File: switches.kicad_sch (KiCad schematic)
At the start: 134 parts

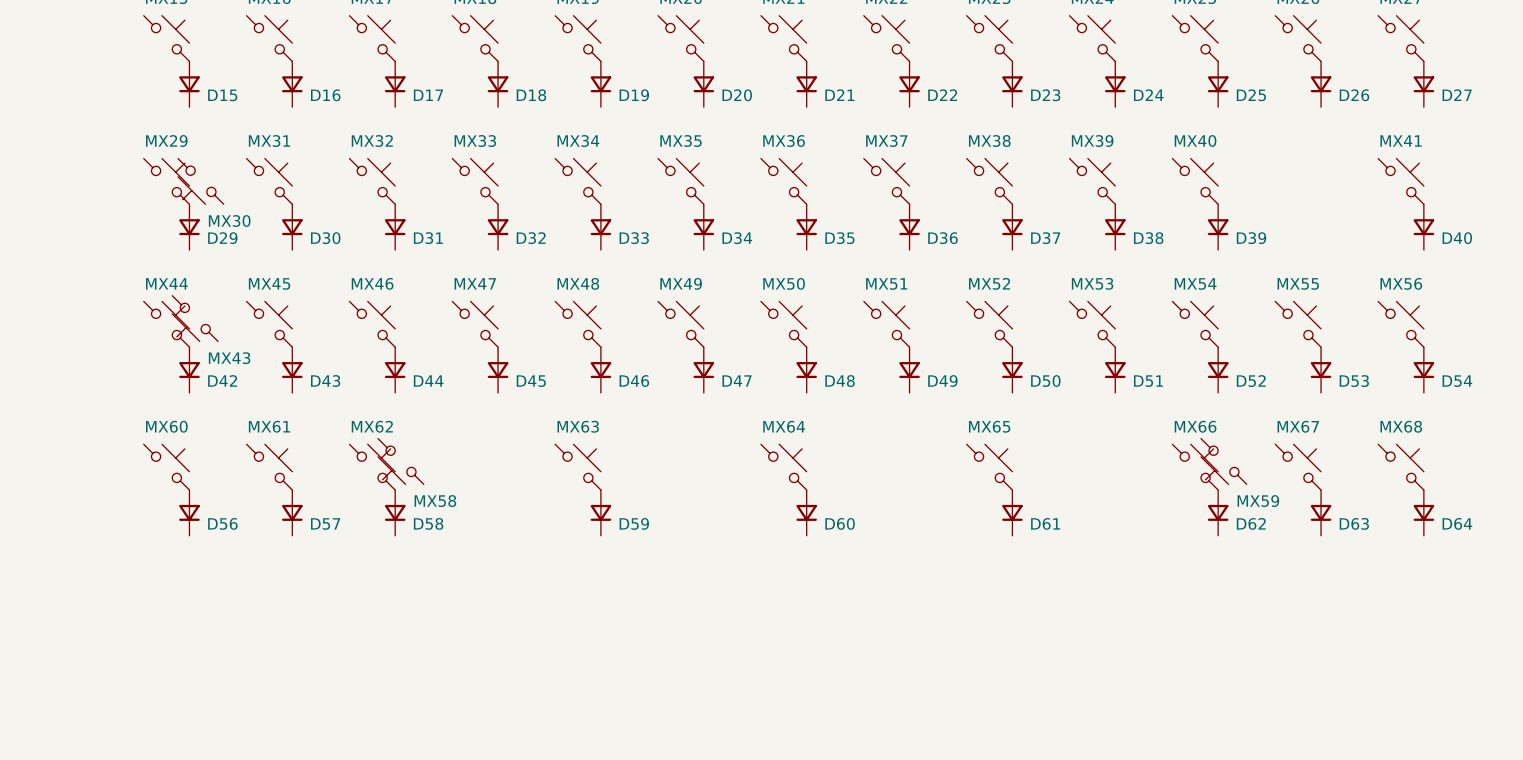
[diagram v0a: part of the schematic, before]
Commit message: Update PCB from schematics
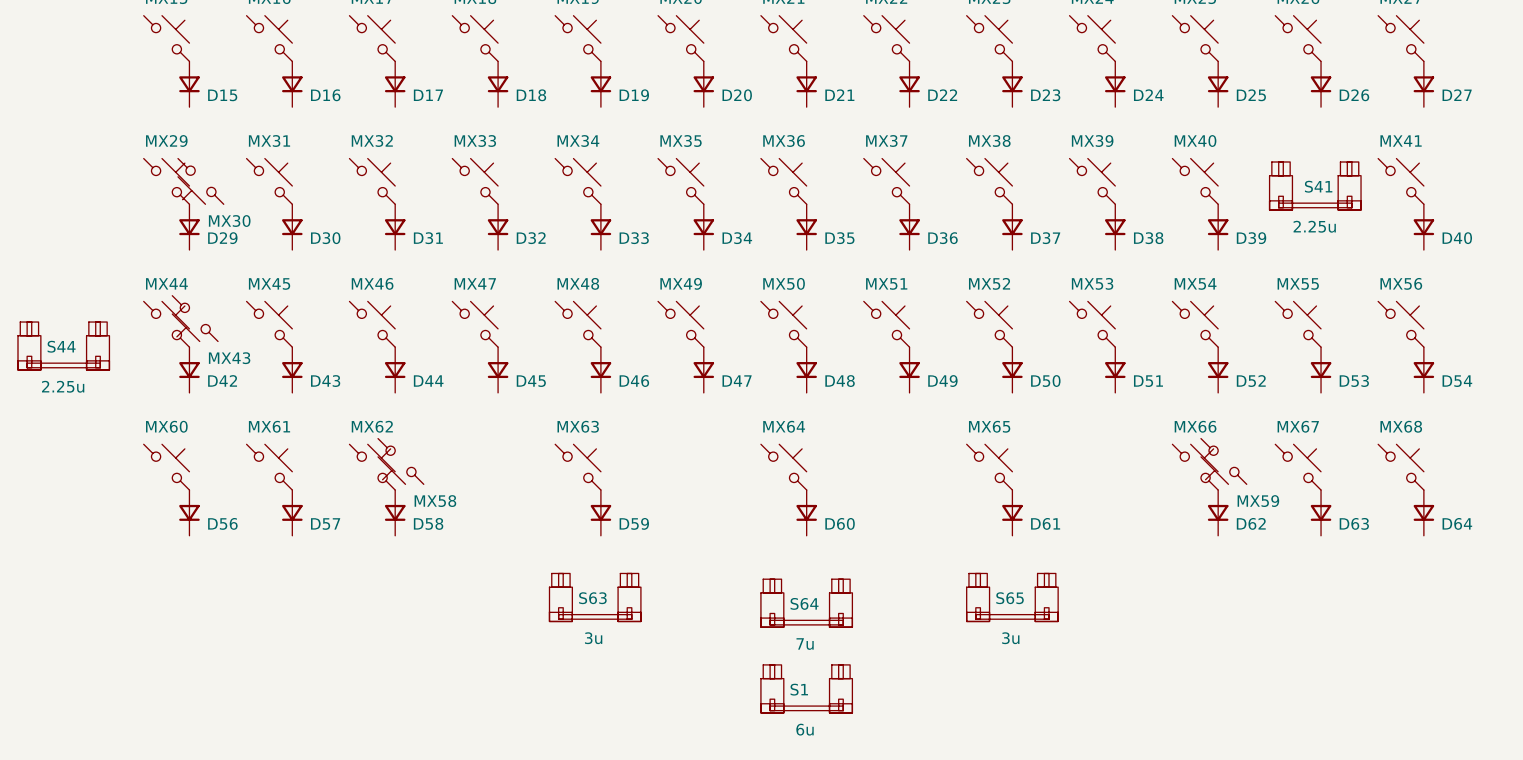
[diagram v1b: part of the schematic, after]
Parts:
- added S1: 6u, PCM_marbastlib-mx:STAB_MX_P_6u, symbol PCM_marbastlib-mx:MX_stab
- added S41, S44: 2.25u, PCM_marbastlib-mx:STAB_MX_P_2.25u, symbol PCM_marbastlib-mx:MX_stab
- added S63, S65: 3u, PCM_marbastlib-mx:STAB_MX_P_3u, symbol PCM_marbastlib-mx:MX_stab
- added S64: 7u, PCM_marbastlib-mx:STAB_MX_P_7u, symbol PCM_marbastlib-mx:MX_stab
- MX15, MX26, MX58, MX59, MX60, MX68: footprint PCM_marbastlib-mx:SW_MX_HS_CPG151101S11_1u -> PCM_marbastlib-mx:SW_MX_HS_CPG151101S11_1.5u
- MX29: footprint PCM_marbastlib-mx:SW_MX_HS_CPG151101S11_1.75u -> PCM_marbastlib-mx:SW_MX_HS_CPG151101S11_1.75u_STP_1.25
- MX30: footprint PCM_marbastlib-mx:SW_MX_HS_CPG151101S11_1.75u_STP_1.5 -> PCM_marbastlib-mx:SW_MX_HS_CPG151101S11_1.75u
- MX43: footprint PCM_marbastlib-mx:SW_MX_HS_CPG151101S11_1u -> PCM_marbastlib-mx:SW_MX_HS_CPG151101S11_1.25u
- MX44: footprint PCM_marbastlib-mx:SW_MX_HS_CPG151101S11_1.25u -> PCM_marbastlib-mx:SW_MX_HS_CPG151101S11_1u
- MX56: footprint PCM_marbastlib-mx:SW_MX_HS_CPG151101S11_1u -> PCM_marbastlib-mx:SW_MX_HS_CPG151101S11_1.75u
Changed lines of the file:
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@@
     )
   )
+  (symbol (lib_id "PCM_marbastlib-mx:MX_stab") (at 193.04 79.375 0) (unit 1)
+    (in_bom yes) (on_board yes) (dnp no)
+    (property "Reference" "S41" (at 191.77 79.375 0)
+      (effects (font (size 1.27 1.27)) (justify left))
+    )
+    (property "Value" "2.25u" (at 190.5 83.82 0)
+      (effects (font (size 1.27 1.27)) (justify left))
+    )
+    (property "Footprint" "PCM_marbastlib-mx:STAB_MX_P_2.25u" (at 193.04 79.375 0)
+      (effects (font (size 1.27 1.27)) hide)
+    )
+    (property "Datasheet" "" (at 193.04 79.375 0)
+      (effects (font (size 1.27 1.27)) hide)
+    )
+    (instances
+      (project "cloak-xt"
+        (path "/4d291fcf-fdf2-46ba-aa57-60bc75f9cc32/1dce68b0-b625-42aa-84db-de4b32ed3fae"
+          (reference "S41") (unit 1)
+        )
+      )
+    )
+  )
   (symbol (lib_id "PCM_marbastlib-mx:MX_SW_HS_CPG151101S11") (at 88.265 46.99 0) (unit 1)
     (in_bom yes) (on_board yes) (dnp no)
@@
       (effects (font (size 1.27 1.27)) hide)
     )
-    (property "Footprint" "PCM_marbastlib-mx:SW_MX_HS_CPG151101S11_1u" (at 202.565 94.615 0)
+    (property "Footprint" "PCM_marbastlib-mx:SW_MX_HS_CPG151101S11_1.75u" (at 202.565 94.615 0)
       (effects (font (size 1.27 1.27)) hide)
     )
@@
       (effects (font (size 1.27 1.27)) hide)
     )
-    (property "Footprint" "PCM_marbastlib-mx:SW_MX_HS_CPG151101S11_1u" (at 191.135 62.865 0)
+    (property "Footprint" "PCM_marbastlib-mx:SW_MX_HS_CPG151101S11_1.5u" (at 191.135 62.865 0)
       (effects (font (size 1.27 1.27)) hide)
     )
@@
     )
   )
+  (symbol (lib_id "PCM_marbastlib-mx:MX_stab") (at 113.03 125.095 0) (unit 1)
+    (in_bom yes) (on_board yes) (dnp no)
+    (property "Reference" "S63" (at 111.125 125.095 0)
+      (effects (font (size 1.27 1.27)) (justify left))
+    )
+    (property "Value" "3u" (at 111.76 129.54 0)
+      (effects (font (size 1.27 1.27)) (justify left))
+    )
+    (property "Footprint" "PCM_marbastlib-mx:STAB_MX_P_3u" (at 113.03 125.095 0)
+      (effects (font (size 1.27 1.27)) hide)
+    )
+    (property "Datasheet" "" (at 113.03 125.095 0)
+      (effects (font (size 1.27 1.27)) hide)
+    )
+    (instances
+      (project "cloak-xt"
+        (path "/4d291fcf-fdf2-46ba-aa57-60bc75f9cc32/1dce68b0-b625-42aa-84db-de4b32ed3fae"
+          (reference "S63") (unit 1)
+        )
+      )
+    )
+  )
+  (symbol (lib_id "PCM_marbastlib-mx:MX_stab") (at 136.525 125.73 0) (unit 1)
+    (in_bom yes) (on_board yes) (dnp no)
+    (property "Reference" "S64" (at 134.62 125.73 0)
+      (effects (font (size 1.27 1.27)) (justify left))
+    )
+    (property "Value" "7u" (at 135.255 130.175 0)
+      (effects (font (size 1.27 1.27)) (justify left))
+    )
+    (property "Footprint" "PCM_marbastlib-mx:STAB_MX_P_7u" (at 136.525 125.73 0)
+      (effects (font (size 1.27 1.27)) hide)
+    )
+    (property "Datasheet" "" (at 136.525 125.73 0)
+      (effects (font (size 1.27 1.27)) hide)
+    )
+    (instances
+      (project "cloak-xt"
+        (path "/4d291fcf-fdf2-46ba-aa57-60bc75f9cc32/1dce68b0-b625-42aa-84db-de4b32ed3fae"
+          (reference "S64") (unit 1)
+        )
+      )
+    )
+  )
   (symbol (lib_id "PCM_marbastlib-mx:MX_SW_HS_CPG151101S11") (at 179.705 110.49 0) (unit 1)
     (in_bom yes) (on_board yes) (dnp no)
@@
       (effects (font (size 1.27 1.27)) hide)
     )
-    (property "Footprint" "PCM_marbastlib-mx:SW_MX_HS_CPG151101S11_1.75u_STP_1.5" (at 69.215 78.74 0)
+    (property "Footprint" "PCM_marbastlib-mx:SW_MX_HS_CPG151101S11_1.75u" (at 69.215 78.74 0)
       (effects (font (size 1.27 1.27)) hide)
     )
@@
       (effects (font (size 1.27 1.27)) hide)
     )
-    (property "Footprint" "PCM_marbastlib-mx:SW_MX_HS_CPG151101S11_1u" (at 202.565 110.49 0)
+    (property "Footprint" "PCM_marbastlib-mx:SW_MX_HS_CPG151101S11_1.5u" (at 202.565 110.49 0)
       (effects (font (size 1.27 1.27)) hide)
     )
@@
       (effects (font (size 1.27 1.27)) hide)
     )
-    (property "Footprint" "PCM_marbastlib-mx:SW_MX_HS_CPG151101S11_1.75u" (at 65.405 78.74 0)
+    (property "Footprint" "PCM_marbastlib-mx:SW_MX_HS_CPG151101S11_1.75u_STP_1.25" (at 65.405 78.74 0)
       (effects (font (size 1.27 1.27)) hide)
     )
@@
       (effects (font (size 1.27 1.27)) hide)
     )
-    (property "Footprint" "PCM_marbastlib-mx:SW_MX_HS_CPG151101S11_1u" (at 68.58 93.98 0)
+    (property "Footprint" "PCM_marbastlib-mx:SW_MX_HS_CPG151101S11_1.25u" (at 68.58 93.98 0)
       (effects (font (size 1.27 1.27)) hide)
     )
@@
       (effects (font (size 1.27 1.27)) hide)
     )
-    (property "Footprint" "PCM_marbastlib-mx:SW_MX_HS_CPG151101S11_1u" (at 65.405 62.865 0)
+    (property "Footprint" "PCM_marbastlib-mx:SW_MX_HS_CPG151101S11_1.5u" (at 65.405 62.865 0)
       (effects (font (size 1.27 1.27)) hide)
     )
@@
       (effects (font (size 1.27 1.27)) hide)
     )
-    (property "Footprint" "PCM_marbastlib-mx:SW_MX_HS_CPG151101S11_1.25u" (at 65.405 94.615 0)
+    (property "Footprint" "PCM_marbastlib-mx:SW_MX_HS_CPG151101S11_1u" (at 65.405 94.615 0)
       (effects (font (size 1.27 1.27)) hide)
     )
@@
       (effects (font (size 1.27 1.27)) hide)
     )
-    (property "Footprint" "PCM_marbastlib-mx:SW_MX_HS_CPG151101S11_1u" (at 182.88 109.855 0)
+    (property "Footprint" "PCM_marbastlib-mx:SW_MX_HS_CPG151101S11_1.5u" (at 182.88 109.855 0)
       (effects (font (size 1.27 1.27)) hide)
     )
@@
     )
   )
+  (symbol (lib_id "PCM_marbastlib-mx:MX_stab") (at 136.525 135.255 0) (unit 1)
+    (in_bom yes) (on_board yes) (dnp no)
+    (property "Reference" "S1" (at 134.62 135.255 0)
+      (effects (font (size 1.27 1.27)) (justify left))
+    )
+    (property "Value" "6u" (at 135.255 139.7 0)
+      (effects (font (size 1.27 1.27)) (justify left))
+    )
+    (property "Footprint" "PCM_marbastlib-mx:STAB_MX_P_6u" (at 136.525 135.255 0)
+      (effects (font (size 1.27 1.27)) hide)
+    )
+    (property "Datasheet" "" (at 136.525 135.255 0)
+      (effects (font (size 1.27 1.27)) hide)
+    )
+    (instances
+      (project "cloak-xt"
+        (path "/4d291fcf-fdf2-46ba-aa57-60bc75f9cc32/1dce68b0-b625-42aa-84db-de4b32ed3fae"
+          (reference "S1") (unit 1)
+        )
+      )
+    )
+  )
   (symbol (lib_id "Device:D_Small") (at 79.375 99.695 90) (unit 1)
     (in_bom yes) (on_board yes) (dnp no)
@@
     )
   )
+  (symbol (lib_id "PCM_marbastlib-mx:MX_stab") (at 53.975 97.155 0) (unit 1)
+    (in_bom yes) (on_board yes) (dnp no)
+    (property "Reference" "S44" (at 52.07 97.155 0)
+      (effects (font (size 1.27 1.27)) (justify left))
+    )
+    (property "Value" "2.25u" (at 51.435 101.6 0)
+      (effects (font (size 1.27 1.27)) (justify left))
+    )
+    (property "Footprint" "PCM_marbastlib-mx:STAB_MX_P_2.25u" (at 53.975 97.155 0)
+      (effects (font (size 1.27 1.27)) hide)
+    )
+    (property "Datasheet" "" (at 53.975 97.155 0)
+      (effects (font (size 1.27 1.27)) hide)
+    )
+    (instances
+      (project "cloak-xt"
+        (path "/4d291fcf-fdf2-46ba-aa57-60bc75f9cc32/1dce68b0-b625-42aa-84db-de4b32ed3fae"
+          (reference "S44") (unit 1)
+        )
+      )
+    )
+  )
   (symbol (lib_id "Device:D_Small") (at 125.095 99.695 90) (unit 1)
     (in_bom yes) (on_board yes) (dnp no)
@@
     )
   )
+  (symbol (lib_id "PCM_marbastlib-mx:MX_stab") (at 159.385 125.095 0) (unit 1)
+    (in_bom yes) (on_board yes) (dnp no)
+    (property "Reference" "S65" (at 157.48 125.095 0)
+      (effects (font (size 1.27 1.27)) (justify left))
+    )
+    (property "Value" "3u" (at 158.115 129.54 0)
+      (effects (font (size 1.27 1.27)) (justify left))
+    )
+    (property "Footprint" "PCM_marbastlib-mx:STAB_MX_P_3u" (at 159.385 125.095 0)
+      (effects (font (size 1.27 1.27)) hide)
+    )
+    (property "Datasheet" "" (at 159.385 125.095 0)
+      (effects (font (size 1.27 1.27)) hide)
+    )
+    (instances
+      (project "cloak-xt"
+        (path "/4d291fcf-fdf2-46ba-aa57-60bc75f9cc32/1dce68b0-b625-42aa-84db-de4b32ed3fae"
+          (reference "S65") (unit 1)
+        )
+      )
+    )
+  )
   (symbol (lib_id "PCM_marbastlib-mx:MX_SW_HS_CPG151101S11") (at 88.265 78.74 0) (unit 1)
     (in_bom yes) (on_board yes) (dnp no)
@@
       (effects (font (size 1.27 1.27)) hide)
     )
-    (property "Footprint" "PCM_marbastlib-mx:SW_MX_HS_CPG151101S11_1u" (at 65.405 110.49 0)
+    (property "Footprint" "PCM_marbastlib-mx:SW_MX_HS_CPG151101S11_1.5u" (at 65.405 110.49 0)
       (effects (font (size 1.27 1.27)) hide)
     )
@@
       (effects (font (size 1.27 1.27)) hide)
     )
-    (property "Footprint" "PCM_marbastlib-mx:SW_MX_HS_CPG151101S11_1u" (at 91.44 109.855 0)
+    (property "Footprint" "PCM_marbastlib-mx:SW_MX_HS_CPG151101S11_1.5u" (at 91.44 109.855 0)
       (effects (font (size 1.27 1.27)) hide)
     )

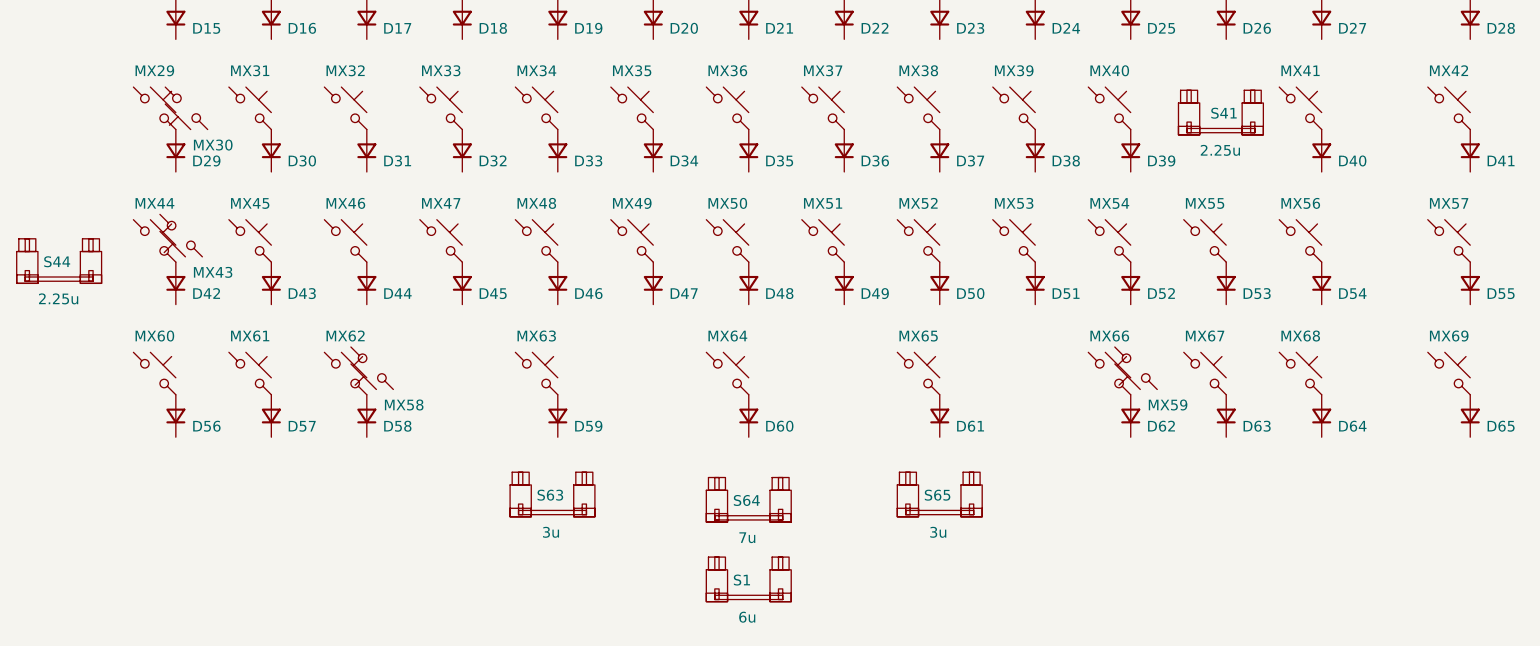
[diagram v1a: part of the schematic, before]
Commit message: Fixed diodes notation
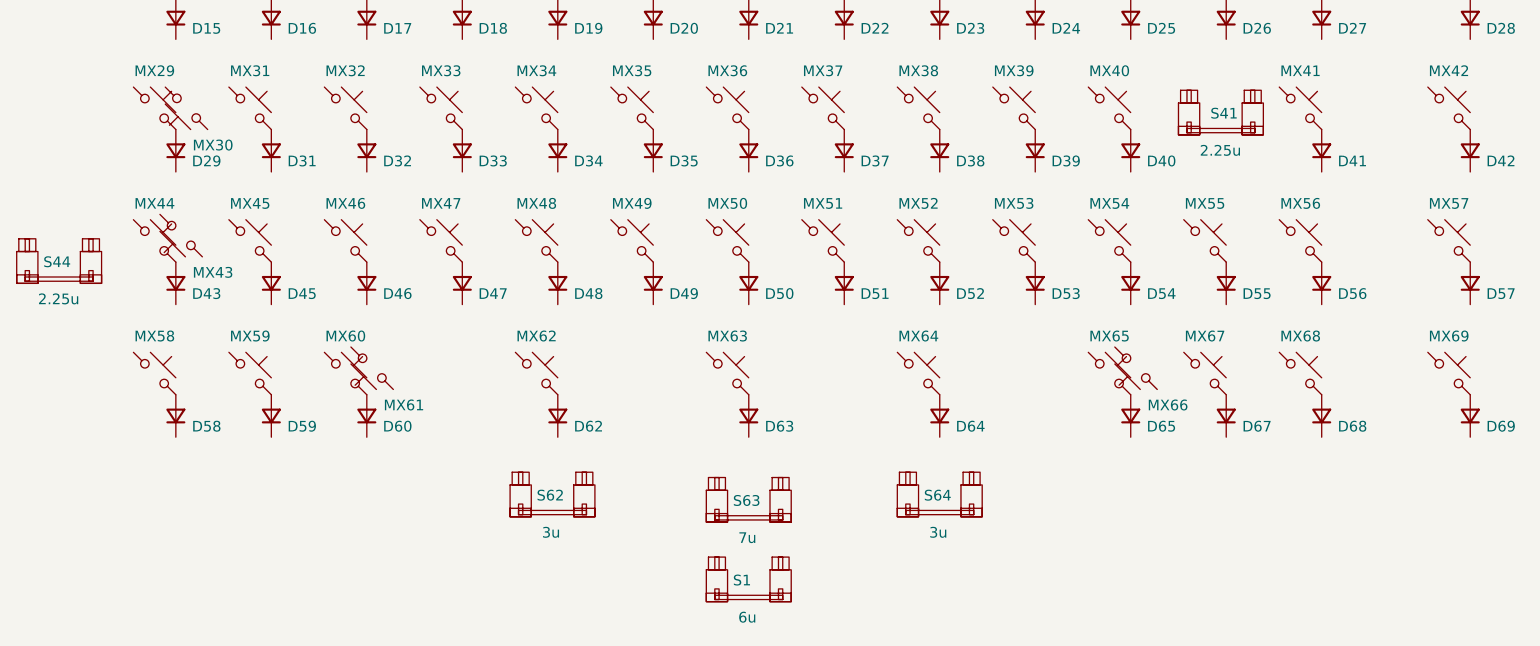
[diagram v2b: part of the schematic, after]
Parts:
- renumbered D30 to D31, D31 to D32, D32 to D33, D33 to D34, D34 to D35, D35 to D36, D36 to D37, D37 to D38, D38 to D39, D39 to D40, D40 to D41, D41 to D42, D42 to D43, D43 to D45, D44 to D46, D45 to D47, D46 to D48, D47 to D49, D48 to D50, D49 to D51, D50 to D52, D51 to D53, D52 to D54, D53 to D55, D54 to D56, D55 to D57, D56 to D58, D57 to D59, D58 to D60, D59 to D62, D60 to D63, D61 to D64, D62 to D65, D63 to D67, D64 to D68, D65 to D69, MX60 to MX58, MX61 to MX59, MX62 to MX60, MX58 to MX61, MX63 to MX62, MX64 to MX63, MX65 to MX64, MX66 to MX65, MX59 to MX66, S63 to S62, S64 to S63, S65 to S64
